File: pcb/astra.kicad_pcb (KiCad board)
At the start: 4 copper layers, 42.6 x 43.4 mm, 88 parts, among them J1 Conn_01x02_Pin, J2 Conn_02x10_Odd_Even, M1 Motor_DC, M2 Motor_DC, M3 Motor_DC, M4 Motor_DC, Q1 AO3400A, Q2 AO3400A, Q3 AO3400A, Q4 AO3400A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

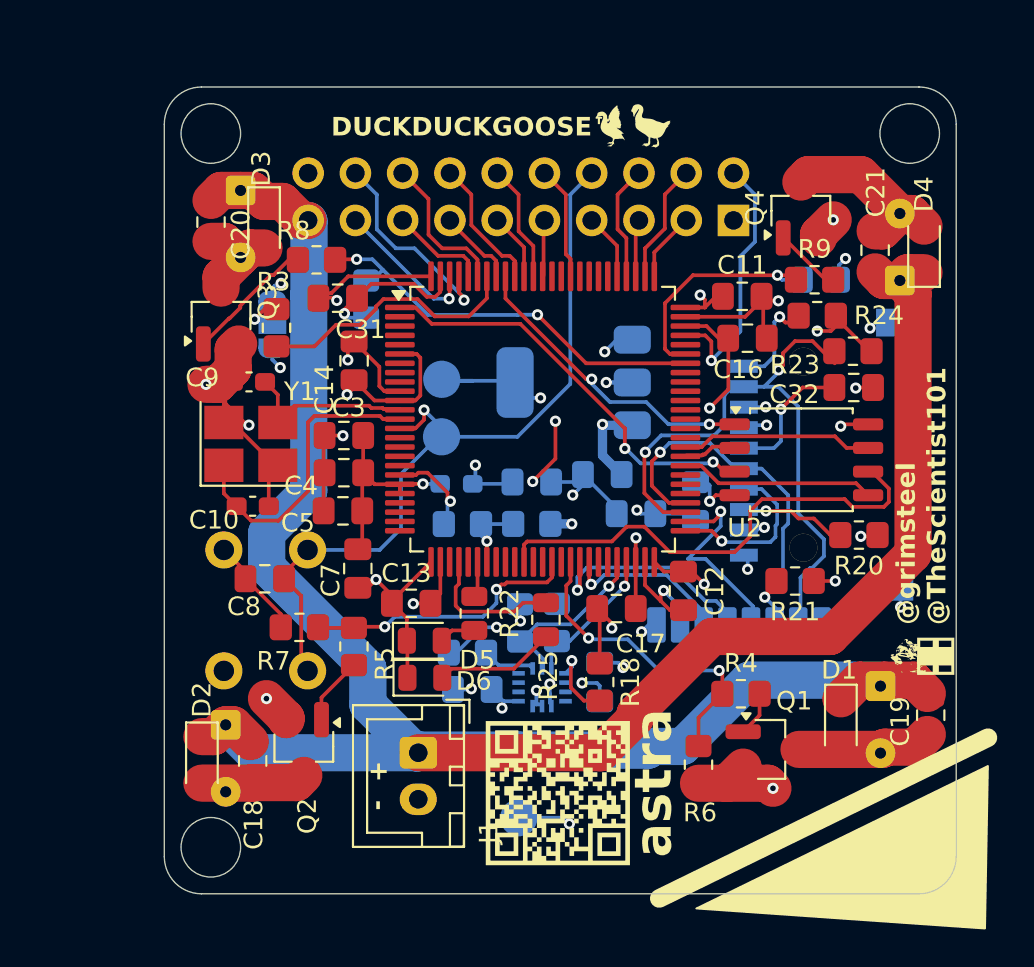
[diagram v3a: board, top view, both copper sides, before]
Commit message: [pcb] utilize unused gpios, silkscreen improvements and [journal] add entry for 7/9
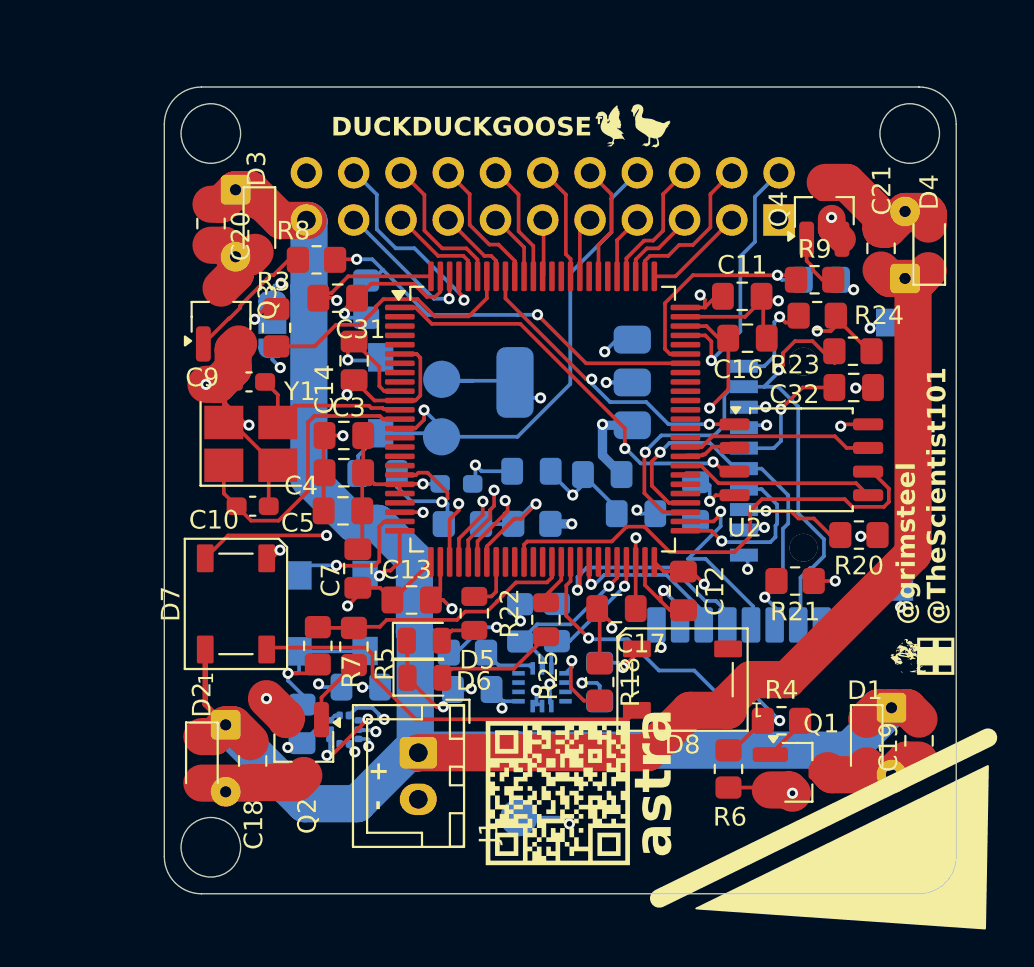
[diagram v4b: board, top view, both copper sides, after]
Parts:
- added C22: 100nF, Capacitor_SMD:C_0805_2012Metric_Pad1.18x1.45mm_HandSolder, B.Cu at (131.7, 71.1)
- added C23: 100nF, Capacitor_SMD:C_0805_2012Metric_Pad1.18x1.45mm_HandSolder, B.Cu at (134.9, 69.1)
- added D7: WS2812B, LED_SMD:LED_WS2812B_PLCC4_5.0x5.0mm_P3.2mm, F.Cu at (128.2, 64.7)
- added D8: WS2812B, LED_SMD:LED_WS2812B_PLCC4_5.0x5.0mm_P3.2mm, F.Cu at (152.2, 68.7)
- added SW1: SW_Push, lcsc:SW-SMD_L4.0-W2.9-LS5.0, B.Cu at (135.1, 65.1)
- added SW3: SW_Push, lcsc:SW-SMD_L4.0-W2.9-LS5.0, B.Cu at (131.5, 65.2)
- added U4: BMP388, Package_LGA:ST_HLGA-10_2x2mm_P0.5mm_LayoutBorder3x2y, B.Cu at (134.0, 71.4)
- C8: moved to B.Cu
- J2: value Conn_02x10_Odd_Even -> Conn_02x11_Odd_Even; footprint Connector_PinHeader_2.54mm:PinHeader_2x10_P2.54mm_Vertical -> Connector_PinHeader_2.54mm:PinHeader_2x11_P2.54mm_Vertical
- SW2: footprint Button_Switch_THT:SW_PUSH_6mm -> lcsc:SW-SMD_L4.0-W2.9-LS5.0
- moved G*** 19.5 mm to (133.5, 76.5)
- moved G*** 15.9 mm to (130.8, 58.9)
- moved SW2 11.8 mm to (135.9, 53.4)
- moved C8 8.29 mm to (135.8, 57.6), turned to 0 degrees
- moved R4 2.62 mm to (157.5, 70.9)
- moved G*** 2.55 mm to (160.2, 42.8)
- moved J2 2.45 mm to (157.3, 44.0)
- moved Q1 1.91 mm to (158.4, 73.7)
- moved D1 1.77 mm to (162.1, 72.1)
- moved R6 1.63 mm to (154.6, 73.5)
- moved C19 1.51 mm to (164.9, 72.0)
- moved R7 1.40 mm to (132.6, 66.9), turned to -90 degrees
- moved M1 1.30 mm to (163.4, 70.2)
- moved Q4 1.26 mm to (159.8, 43.5)
- moved C2 0.58 mm to (144.0, 57.5)
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- renumbered VCC to TP1, GND to TP4
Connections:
- J2 pad 10: DDG_MAGIC_2 -> DDG_MAGIC_8
- J2 pad 11: TRST -> DDG_MAGIC_1
- J2 pad 12: TDO -> DDG_MAGIC_2
- J2 pad 13: DDG_MAGIC_3 -> TRST
- J2 pad 14: DDG_MAGIC_4 -> TDO
- J2 pad 15: I2C1_SDA -> DDG_MAGIC_3
- J2 pad 16: I2C1_SCK -> DDG_MAGIC_4
- J2 pad 17: DDG_MAGIC_5 -> I2C1_SDA
- J2 pad 18: DDG_MAGIC_6 -> I2C1_SCK
- J2 pad 19: +BATT -> DDG_MAGIC_5
- J2 pad 20: +3.3V -> DDG_MAGIC_6
- J2 pad 9: DDG_MAGIC_1 -> DDG_MAGIC_7
- U3 pad 23: unconnected-(U3-PA1-Pad23) -> NEOPIXEL
- U3 pad 24: unconnected-(U3-PA2-Pad24) -> BTN2
- U3 pad 25: unconnected-(U3-PA3-Pad25) -> BTN1
- U3 pad 28: unconnected-(U3-PA4-Pad28) -> BAR_CS
- U3 pad 29: STATUS_LED_2 -> SPI1_CLK
- U3 pad 30: unconnected-(U3-PA6-Pad30) -> SPI1_MISO
- U3 pad 31: STATUS_LED_1 -> SPI1_MOSI
- U3 pad 33: unconnected-(U3-PC5-Pad33) -> STATUS_LED_1
- U3 pad 40: unconnected-(U3-PE10-Pad40) -> STATUS_LED_2
- U3 pad 82: unconnected-(U3-PD1-Pad82) -> DDG_MAGIC_8
- U3 pad 84: unconnected-(U3-PD3-Pad84) -> DDG_MAGIC_7
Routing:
- net SPI1_MISO: track 0.00 -> 24.4 mm, vias 0 -> 2
- net Net-(D7-DOUT): track 0.00 -> 22.4 mm
- net BAR_CS: track 0.00 -> 21.9 mm, vias 0 -> 2
- net SPI1_MOSI: track 0.00 -> 21.0 mm, vias 0 -> 2
- net SPI1_CLK: track 0.00 -> 20.2 mm, vias 0 -> 2
- net GND: track 102.6 -> 117.2 mm, vias 30 -> 34
- net NEOPIXEL: track 0.00 -> 14.0 mm, vias 0 -> 2
- net RST: track 41.3 -> 30.3 mm
- net BTN2: track 0.00 -> 7.73 mm, vias 0 -> 1
- net DDG_MAGIC_8: track 0.00 -> 6.33 mm
- net +BATT: track 163.7 -> 170.0 mm
- net +3.3V: track 64.9 -> 70.6 mm, vias 21 -> 23
- net STATUS_LED_2: track 7.60 -> 2.53 mm
- net BAT_MEASURE: track 3.28 -> 7.81 mm
- net BTN1: track 0.00 -> 3.85 mm, vias 0 -> 1
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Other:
- board text added: "D1"
- board text added: "D3"
- board text added: "MOSI"
- board text removed: "MO"

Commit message: [pcb] some more silkscreen improvements
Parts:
- moved G*** 2.79 mm to (129.6, 56.4)
- renumbered TP4 to GND, TP1 to VCC
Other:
- board text added: "BTN 1"
- board text added: "BTN 2"
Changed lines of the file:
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@@
 		(at 131.54 65.16 90)
 		(property "Reference" "SW3"
-			(at 0 4 90)
+			(at 0 0 270)
 			(layer "B.SilkS")
 			(effects
@@
 		(tags "capacitor handsolder")
 		(property "Reference" "C30"
-			(at 3.65 -0.12 0)
+			(at 0.28 -1.42 0)
 			(layer "B.SilkS")
 			(effects
@@
 		(tags "capacitor handsolder")
 		(property "Reference" "C23"
-			(at 0 1.68 0)
+			(at 2.57 1.9 0)
 			(layer "B.SilkS")
 			(effects
@@
 		(tags "connector wire 0.1sqmm")
 		(property "Reference" "M1"
-			(at -1.99 0.12 0)
+			(at 1.7 0.07 270)
+			(unlocked yes)
 			(layer "B.SilkS")
 			(effects
@@
 		(tags "connector wire 0.1sqmm")
 		(property "Reference" "M2"
-			(at 1.75 2.1 270)
+			(at 1.8 0 270)
 			(unlocked yes)
 			(layer "B.SilkS")
@@
 		(descr "SMD pad as test Point, diameter 2.0mm")
 		(tags "test point SMD pad")
-		(property "Reference" "TP4"
+		(property "Reference" "GND"
 			(at 2.67 -0.24 270)
 			(unlocked yes)
@@
 		(tags "ST HLGA NoLead")
 		(property "Reference" "U4"
-			(at 0 1.95 90)
+			(at 0.9 -2.0075 270)
+			(unlocked yes)
 			(layer "B.SilkS")
 			(effects
@@
 		(tags "connector wire 0.1sqmm")
 		(property "Reference" "M4"
-			(at 3.56 -2.12 90)
+			(at 1.79 0.01 270)
+			(unlocked yes)
 			(layer "B.SilkS")
 			(effects
@@
 		(tags "capacitor handsolder")
 		(property "Reference" "C22"
-			(at 0 1.68 90)
+			(at 0.18 1.83 270)
+			(unlocked yes)
 			(layer "B.SilkS")
 			(effects
@@
 	(footprint "LOGO"
 		(layer "B.Cu")
-		(at 130.816636 58.875399 90)
+		(at 129.626636 56.355399 90)
 		(property "Reference" "G***"
 			(at 0 0 90)
@@
 		(at 135.09 65.14 90)
 		(property "Reference" "SW1"
-			(at 0 4 90)
+			(at 0 0 270)
 			(layer "B.SilkS")
 			(effects
@@
 		(descr "SMD pad as test Point, diameter 2.0mm")
 		(tags "test point SMD pad")
-		(property "Reference" "TP1"
+		(property "Reference" "VCC"
 			(at 2.71 -0.01 270)
 			(unlocked yes)
@@
 		)
 	)
+	(gr_text "BTN 2"
+		(at 128.4 65.96 270)
+		(layer "B.SilkS")
+		(effects
+			(font
+				(face "Cantarell")
+				(size 1 1)
+				(thickness 0.25)
+				(bold yes)
+			)
+			(justify left bottom mirror)
+		)
+		(render_cache "BTN 2" 270
+			(polygon
+				(pts
+					(xy 128.57 65.846243) (xy 128.57 65.483115) (xy 128.571933 65.431944) (xy 128.577652 65.383855)
+					(xy 128.586725 65.340207) (xy 128.599147 65.299753) (xy 128.61424 65.263799) (xy 128.632259 65.231086)
+					(xy 128.652367 65.202657) (xy 128.675024 65.177488) (xy 128.69943 65.156233) (xy 128.726078 65.138275)
+					(xy 128.754444 65.123907) (xy 128.784824 65.112942) (xy 128.851332 65.101611) (xy 128.870662 65.101058)
+					(xy 128.906227 65.102994) (xy 128.939723 65.108726) (xy 128.970401 65.117902) (xy 128.998912 65.130502)
+					(xy 129.024911 65.146244) (xy 129.048605 65.165138) (xy 129.088904 65.212249) (xy 129.119274 65.272128)
+					(xy 129.138415 65.345322) (xy 129.144459 65.42407) (xy 129.144459 65.731877) (xy 129.003775 65.731877)
+					(xy 129.003775 65.457409) (xy 129.001851 65.426406) (xy 128.996203 65.398096) (xy 128.987367 65.373425)
+					(xy 128.975382 65.351576) (xy 128.960854 65.333164) (xy 128.943655 65.317701) (xy 128.902274 65.296302)
+					(xy 128.85148 65.288068) (xy 128.847337 65.288026) (xy 128.819482 65.289992) (xy 128.795076 65.295934)
+					(xy 128.77622 65.304618) (xy 128.760006 65.31655) (xy 128.73601 65.348983) (xy 128.720887 65.396903)
+					(xy 128.715874 65.459851) (xy 128.715874 65.667824) (xy 129.397128 65.667824) (xy 129.397128 65.538375)
+					(xy 129.395189 65.500251) (xy 129.389436 65.466503) (xy 129.380914 65.439569) (xy 129.36935 65.416473)
+					(xy 129.356043 65.39864) (xy 129.340262 65.384215) (xy 129.30319 65.366311) (xy 129.265542 65.361543)
+					(xy 129.241579 65.363518) (xy 129.219417 65.369524) (xy 129.200262 65.378877) (xy 129.182494 65.39195)
+					(xy 129.150085 65.430731) (xy 129.119926 65.492645) (xy 129.113623 65.510043) (xy 129.094267 65.332051)
+					(xy 129.119489 65.279983) (xy 129.157446 65.236263) (xy 129.206327 65.203339) (xy 129.234019 65.191729)
+					(xy 129.263358 65.183709) (xy 129.311582 65.17885) (xy 129.34331 65.180796) (xy 129.372831 65.186603)
+					(xy 129.398982 65.195731) (xy 129.423052 65.208309) (xy 129.464359 65.24312) (xy 129.497861 65.292127)
+					(xy 129.523298 65.357885) (xy 129.539089 65.443721) (xy 129.543063 65.524392) (xy 129.543063 65.846243)
+				)
+			)
+			(polygon
+				(pts
+					(xy 128.57 64.727367) (xy 128.57 64.548948) (xy 129.384977 64.548948) (xy 129.384977 64.235584)
+					(xy 129.543063 64.235584) (xy 129.543063 65.038593) (xy 129.384977 65.038593) (xy 129.384977 64.727367)
+				)
+			)
+			(polygon
+				(pts
+					(xy 128.57 64.110165) (xy 128.57 63.939439) (xy 129.328679 63.939439) (xy 129.321535 63.95617)
+					(xy 128.57 63.462311) (xy 128.57 63.260566) (xy 129.543063 63.260566) (xy 129.543063 63.432697)
+					(xy 128.77724 63.434162) (xy 128.784384 63.411753) (xy 129.543063 63.903475) (xy 129.543063 64.110165)
+				)
+			)
+			(polygon
+				(pts
+					(xy 128.57 62.789849) (xy 128.57 62.138087) (xy 128.726559 62.138087) (xy 128.726559 62.585662)
+					(xy 128.684122 62.577419) (xy 128.764084 62.486174) (xy 128.838843 62.407456) (xy 128.899299 62.349602)
+					(xy 128.956849 62.300343) (xy 129.005969 62.263498) (xy 129.05342 62.233037) (xy 129.095725 62.210544)
+					(xy 129.137108 62.1931) (xy 129.175643 62.181098) (xy 129.213753 62.173353) (xy 129.266885 62.169412)
+					(xy 129.303377 62.171344) (xy 129.337816 62.177058) (xy 129.369592 62.186243) (xy 129.399191 62.198842)
+					(xy 129.42634 62.214615) (xy 129.451155 62.233517) (xy 129.49362 62.280529) (xy 129.525974 62.33986)
+					(xy 129.546956 62.411662) (xy 129.554776 62.495856) (xy 129.554787 62.4992) (xy 129.55285 62.544801)
+					(xy 129.547106 62.589323) (xy 129.537616 62.632663) (xy 129.524495 62.674391) (xy 129.50796 62.714006)
+					(xy 129.488041 62.751511) (xy 129.441275 62.815983) (xy 129.310788 62.768722) (xy 129.355372 62.696856)
+					(xy 129.371957 62.659417) (xy 129.384321 62.622134) (xy 129.392464 62.585457) (xy 129.396379 62.54986)
+					(xy 129.396762 62.535165) (xy 129.394839 62.502745) (xy 129.3892 62.47307) (xy 129.38036 62.447079)
+					(xy 129.368377 62.423999) (xy 129.353903 62.404533) (xy 129.33679 62.38811) (xy 129.317542 62.375072)
+					(xy 129.296047 62.36526) (xy 129.246731 62.355875) (xy 129.238675 62.355708) (xy 129.183104 62.363603)
+					(xy 129.121827 62.388762) (xy 129.048222 62.436711) (xy 128.952691 62.518451) (xy 128.817401 62.655413)
+					(xy 128.69493 62.789849)
+				)
+			)
+		)
+	)
 	(gr_text "RST"
 		(at 140.73 56.95 270)
@@
 				)
 			)
+		)
+	)
+	(gr_text "BTN 1"
+		(at 136.94 65.89 270)
+		(layer "B.SilkS")
+		(effects
+			(font
+				(face "Cantarell")
+				(size 1 1)
+				(thickness 0.25)
+				(bold yes)
+			)
+			(justify left bottom mirror)
+		)
+		(render_cache "BTN 1" 270
+			(polygon
+				(pts
+					(xy 137.11 65.776243) (xy 137.11 65.413115) (xy 137.111933 65.361944) (xy 137.117652 65.313855)
+					(xy 137.126725 65.270207) (xy 137.139147 65.229753) (xy 137.15424 65.193799) (xy 137.172259 65.161086)
+					(xy 137.192367 65.132657) (xy 137.215024 65.107488) (xy 137.23943 65.086233) (xy 137.266078 65.068275)
+					(xy 137.294444 65.053907) (xy 137.324824 65.042942) (xy 137.391332 65.031611) (xy 137.410662 65.031058)
+					(xy 137.446227 65.032994) (xy 137.479723 65.038726) (xy 137.510401 65.047902) (xy 137.538912 65.060502)
+					(xy 137.564911 65.076244) (xy 137.588605 65.095138) (xy 137.628904 65.142249) (xy 137.659274 65.202128)
+					(xy 137.678415 65.275322) (xy 137.684459 65.35407) (xy 137.684459 65.661877) (xy 137.543775 65.661877)
+					(xy 137.543775 65.387409) (xy 137.541851 65.356406) (xy 137.536203 65.328096) (xy 137.527367 65.303425)
+					(xy 137.515382 65.281576) (xy 137.500854 65.263164) (xy 137.483655 65.247701) (xy 137.442274 65.226302)
+					(xy 137.39148 65.218068) (xy 137.387337 65.218026) (xy 137.359482 65.219992) (xy 137.335076 65.225934)
+					(xy 137.31622 65.234618) (xy 137.300006 65.24655) (xy 137.27601 65.278983) (xy 137.260887 65.326903)
+					(xy 137.255874 65.389851) (xy 137.255874 65.597824) (xy 137.937128 65.597824) (xy 137.937128 65.468375)
+					(xy 137.935189 65.430251) (xy 137.929436 65.396503) (xy 137.920914 65.369569) (xy 137.90935 65.346473)
+					(xy 137.896043 65.32864) (xy 137.880262 65.314215) (xy 137.84319 65.296311) (xy 137.805542 65.291543)
+					(xy 137.781579 65.293518) (xy 137.759417 65.299524) (xy 137.740262 65.308877) (xy 137.722494 65.32195)
+					(xy 137.690085 65.360731) (xy 137.659926 65.422645) (xy 137.653623 65.440043) (xy 137.634267 65.262051)
+					(xy 137.659489 65.209983) (xy 137.697446 65.166263) (xy 137.746327 65.133339) (xy 137.774019 65.121729)
+					(xy 137.803358 65.113709) (xy 137.851582 65.10885) (xy 137.88331 65.110796) (xy 137.912831 65.116603)
+					(xy 137.938982 65.125731) (xy 137.963052 65.138309) (xy 138.004359 65.17312) (xy 138.037861 65.222127)
+					(xy 138.063298 65.287885) (xy 138.079089 65.373721) (xy 138.083063 65.454392) (xy 138.083063 65.776243)
+				)
+			)
+			(polygon
+				(pts
+					(xy 137.11 64.657367) (xy 137.11 64.478948) (xy 137.924977 64.478948) (xy 137.924977 64.165584)
+					(xy 138.083063 64.165584) (xy 138.083063 64.968593) (xy 137.924977 64.968593) (xy 137.924977 64.657367)
+				)
+			)
+			(polygon
+				(pts
+					(xy 137.11 64.040165) (xy 137.11 63.869439) (xy 137.868679 63.869439) (xy 137.861535 63.88617)
+					(xy 137.11 63.392311) (xy 137.11 63.190566) (xy 138.083063 63.190566) (xy 138.083063 63.362697)
+					(xy 137.31724 63.364162) (xy 137.324384 63.341753) (xy 138.083063 63.833475) (xy 138.083063 64.040165)
+				)
+			)
+			(polygon
+				(pts
+					(xy 137.106092 62.474202) (xy 137.106092 62.296332) (xy 138.083063 62.296332) (xy 138.083063 62.402883)
+					(xy 137.895607 62.771568) (xy 137.767562 62.704523) (xy 137.896339 62.417782) (xy 137.952943 62.474202)
+				)
+			)

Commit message: [pcb] switch bmi270 to SPI, wire interrupt pins and SD chip detect
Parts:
- removed the G*** at (129.6, 56.4)
- removed R16, R17: 2.2k, Resistor_SMD:R_0805_2012Metric_Pad1.20x1.40mm_HandSolder
- removed R18, R19: 100k, Resistor_SMD:R_0805_2012Metric_Pad1.20x1.40mm_HandSolder
- added J3: Conn_01x04_MountingPin, Connector_JST:JST_SH_BM04B-SRSS-TB_1x04-1MP_P1.00mm_Vertical, B.Cu at (128.8, 57.3)
- moved R25 4.15 mm to (142.2, 68.7), turned to 0 degrees
- moved C17 3.53 mm to (147.7, 68.3), turned to 90 degrees
- moved U7 3.50 mm to (144.7, 65.6)
- moved C29 2.45 mm to (145.3, 68.2), turned to 180 degrees
- moved C30 1.93 mm to (141.8, 67.6), turned to -90 degrees
- moved FB1 1.74 mm to (141.1, 56.9), turned to -90 degrees
- moved TP3 1.58 mm to (139.3, 54.1)
- moved TP2 1.54 mm to (139.2, 51.0)
- renumbered VCC to TP1, GND to TP4
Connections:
- net CS_SD renamed SD_CS
- U3 pad 18: unconnected-(U3-PC3_C-Pad18) -> NEOPIXEL
- U3 pad 22: unconnected-(U3-PA0-Pad22) -> UART4_TX
- U3 pad 23: NEOPIXEL -> UART4_RX
- U3 pad 37: unconnected-(U3-PE7-Pad37) -> IMU_INT1
- U3 pad 42: NRF_CS -> SPI4_SCK
- U3 pad 43: NRF_CE -> SPI4_MISO
- U3 pad 44: unconnected-(U3-PE14-Pad44) -> SPI4_MOSI
- U3 pad 45: unconnected-(U3-PE15-Pad45) -> IMU_CS
- U3 pad 46: IMU_SCL -> NRF_CE
- U3 pad 47: IMU_SDA -> NRF_CS
- U3 pad 55: unconnected-(U3-PD8-Pad55) -> SD_CD
- U3 pad 64: unconnected-(U3-PC7-Pad64) -> NRF_IRQ
- U3 pad 82: DDG_MAGIC_8 -> unconnected-(U3-PD1-Pad82)
- U3 pad 84: DDG_MAGIC_7 -> DDG_MAGIC_8
- U3 pad 85: DDG_MAGIC_2 -> DDG_MAGIC_7
- U3 pad 86: unconnected-(U3-PD5-Pad86) -> DDG_MAGIC_2
- U3 pad 87: unconnected-(U3-PD6-Pad87) -> DDG_MAGIC_1
- U3 pad 88: DDG_MAGIC_1 -> unconnected-(U3-PD7-Pad88)
- U5 pad 8: unconnected-(U5-IRQ-Pad8) -> NRF_IRQ
- U7 pad 1: Net-(U7-SDO) -> SPI4_MISO
- U7 pad 12: Net-(U7-CSB) -> IMU_CS
- U7 pad 13: IMU_SCL -> SPI4_SCK
- U7 pad 14: IMU_SDA -> SPI4_MOSI
- U7 pad 4: unconnected-(U7-INT1-Pad4) -> IMU_INT1
- U8 pad 9: GND -> SD_CD
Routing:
- net IMU_INT1: track 0.00 -> 19.5 mm, vias 0 -> 1
- net NRF_IRQ: track 0.00 -> 18.6 mm, vias 0 -> 1
- net UART4_RX: track 0.00 -> 12.9 mm, vias 0 -> 2
- net UART4_TX: track 0.00 -> 12.8 mm, vias 0 -> 2
- net IMU_SCL: track 9.41 -> 0.00 mm, vias 1 -> 0
- net IMU_CS: track 0.00 -> 9.07 mm, vias 0 -> 1
- net IMU_SDA: track 7.46 -> 0.00 mm, vias 1 -> 0
- net SPI4_MOSI: track 0.00 -> 7.39 mm, vias 0 -> 1
- net GND: track 117.2 -> 124.3 mm, vias 34 -> 37
- net STATUS_LED_2: track 2.53 -> 7.49 mm
- net Net-(D6-A): track 6.48 -> 2.09 mm
- net +3.3V: track 70.6 -> 66.3 mm, vias 23 -> 20
- net SPI4_SCK: track 0.00 -> 4.23 mm, vias 0 -> 1
- net Net-(U7-SDO): track 4.13 -> 0.00 mm, vias 1 -> 0
- net SD_CD: track 0.00 -> 4.06 mm, vias 0 -> 1
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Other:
- board text added: "RX"
- board text added: "TX"
- board text removed: "D4"
- board text removed: "D7"
